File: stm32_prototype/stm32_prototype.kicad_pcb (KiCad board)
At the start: 2 copper layers, 53.3 x 22.9 mm, 48 parts, among them J1 USB-C, J2 Cortex-Debug, J3 SWD, J4 Qwiic, J5 Header_A, J6 Header_B, SW1 BOOT0, SW2 RESET, U1 STM32F103C8T6, U2 USBLC6-2SC6, U3 AP2112K-3.3, Y1 8MHz, Y2 32.768kHz

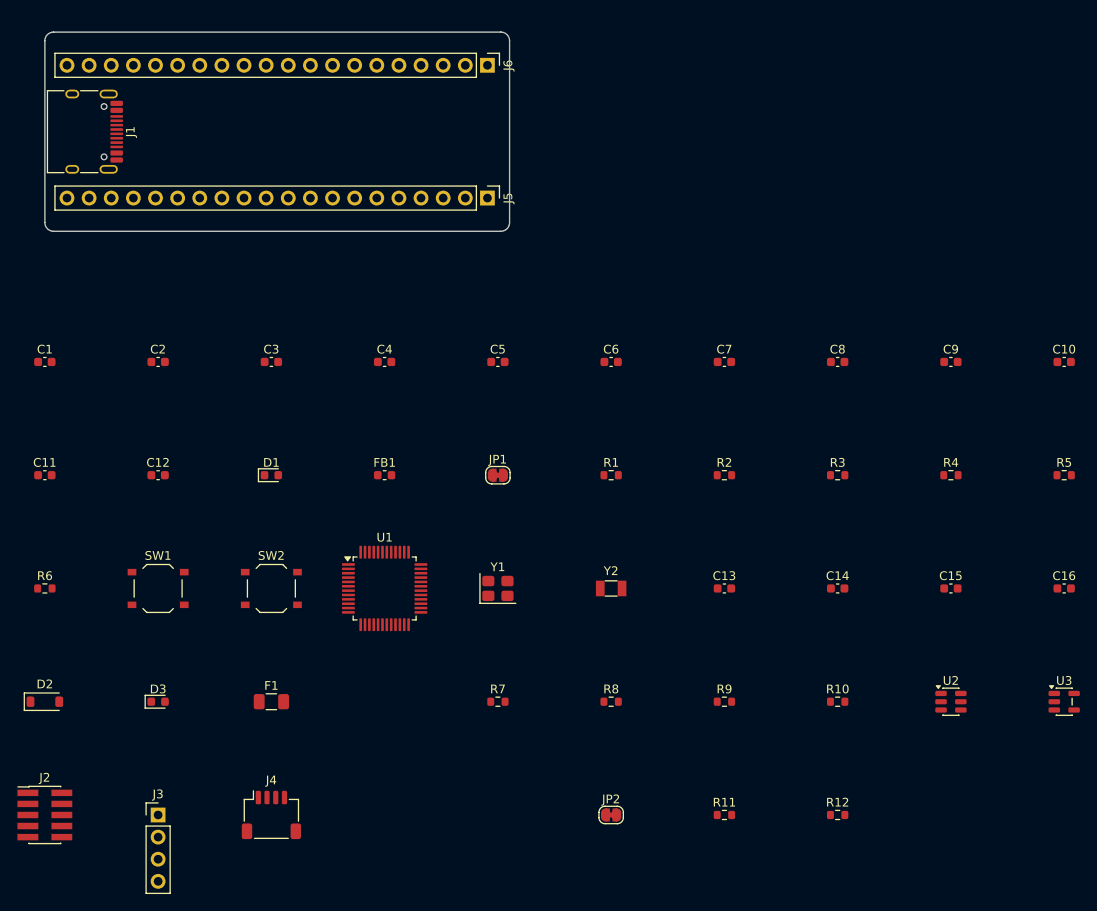
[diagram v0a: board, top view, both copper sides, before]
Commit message: Rev B placement: 76.2 x 22.86 mm board with Blue-Pill header pinout
- Headers centred; USB-C, ESD and power path in the left extension,
  Cortex-Debug, SWD and Qwiic in the right extension
- MCU rotated so PA11/PA12 face the USB connector; decoupling within 2-4 mm of
  the VDD pins, HSE crystal 3-5 mm from PD0/PD1
- Silk designators only on connectors, buttons, ICs and LEDs
- scripts/place_revb.py reproduces the placement

Co-Authored-By: Claude Opus 5.5 (1M context) <noreply@anthropic.com>
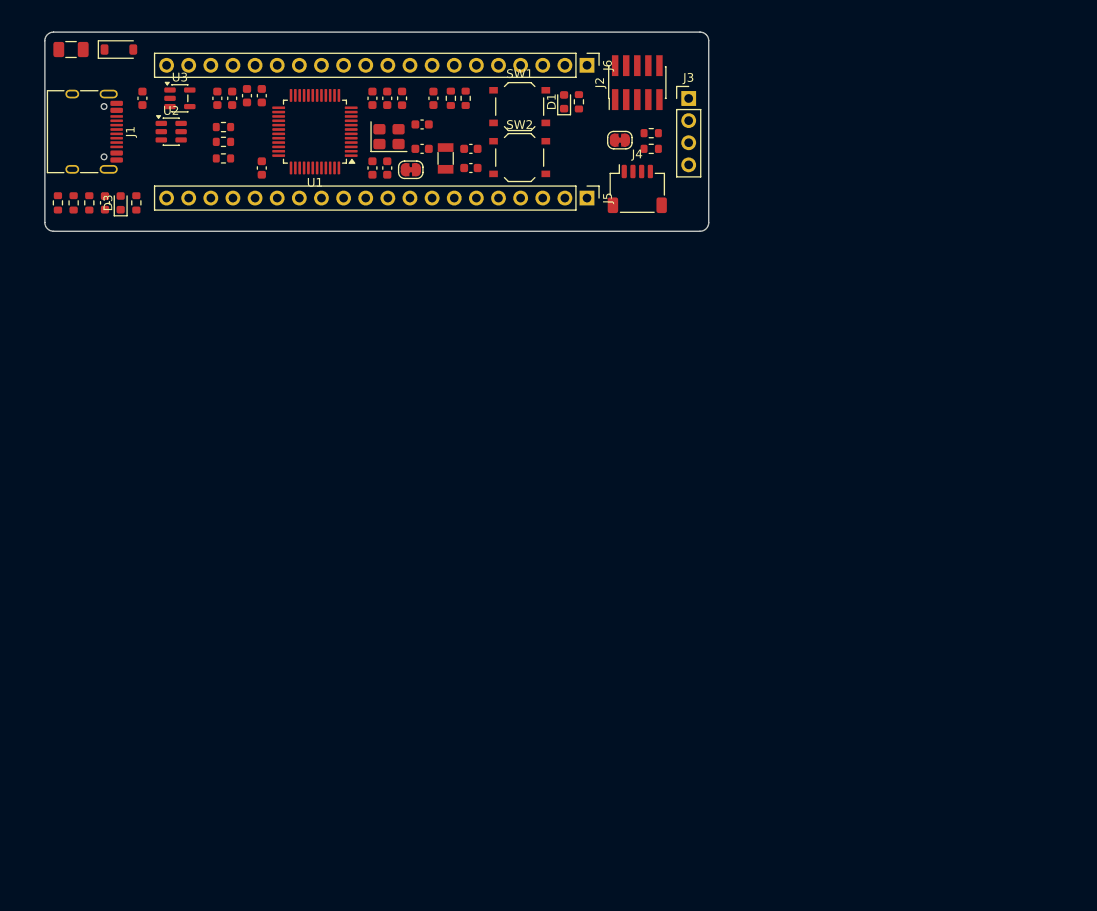
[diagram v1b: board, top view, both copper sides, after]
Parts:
- moved U3 122.9 mm to (115.5, 107.6)
- moved U2 110.9 mm to (114.5, 111.4)
- moved C16 110.8 mm to (121.5, 107.6), turned to 90 degrees
- moved J2 108.1 mm to (168.0, 105.8), turned to 90 degrees
- moved R5 103.8 mm to (120.5, 112.6)
- moved J3 102.3 mm to (173.9, 107.6)
- moved C15 101.3 mm to (119.8, 107.6), turned to 90 degrees
- moved R10 98.8 mm to (110.5, 119.6), turned to 90 degrees
- moved C14 97.6 mm to (111.2, 107.6), turned to 90 degrees
- moved R9 92.7 mm to (105.1, 119.6), turned to 90 degrees
- moved R4 92.6 mm to (120.5, 110.9)
- moved R8 84.2 mm to (103.3, 119.6), turned to 90 degrees
- moved C13 83.8 mm to (106.9, 119.6), turned to 90 degrees
- moved J4 83.2 mm to (168.0, 118.0)
- moved R12 79.4 mm to (169.6, 113.4)
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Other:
- board size 53.3 x 22.9 mm -> 76.2 x 22.9 mm

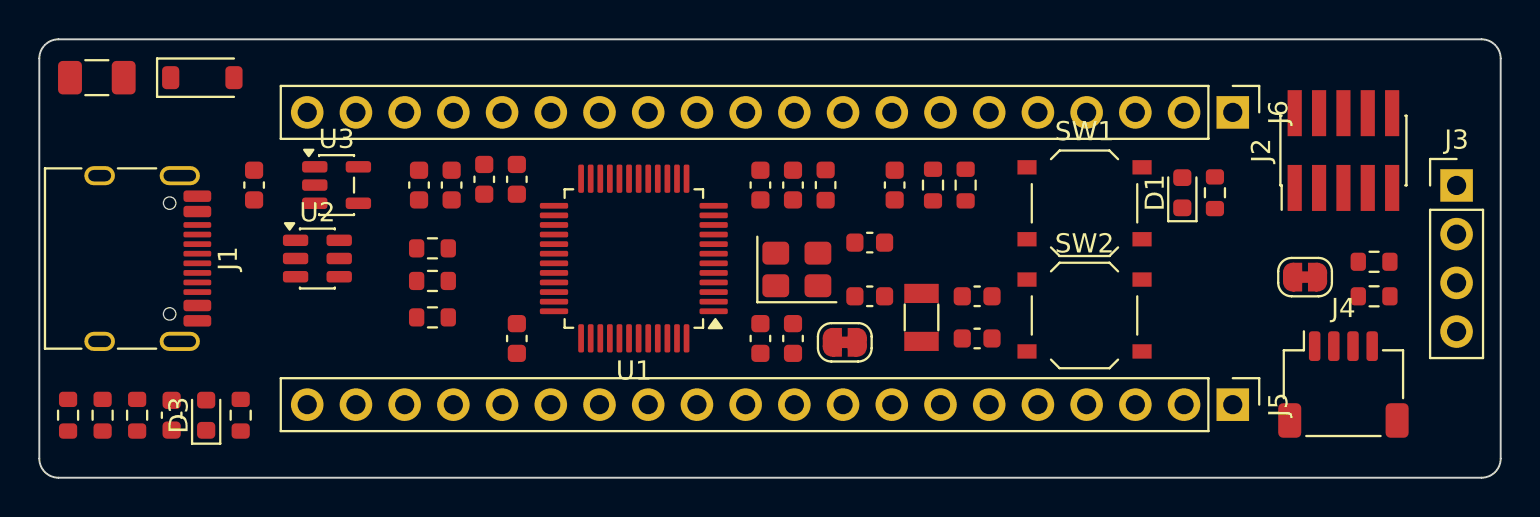
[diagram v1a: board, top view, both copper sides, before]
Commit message: Rev B routing: 4 layers SIG/GND/GND/SIG, Freerouting, GND pours, bottom pinout silk
- Freerouting 2.5 routes F.Cu/B.Cu with GND as a plane; vias modelled 0.7 mm so
  JLC's 0.5 mm hole-to-hole rule holds; board then converted to 4 layers with
  solid GND planes on In1/In2 and GND pours + edge stitching on F.Cu/B.Cu
- Net classes: Default/Supply clearance 0.15 mm (LQFP escape between the header rows),
  Supply class 0.3 mm for 3V3/GND/VDDA/VBAT
- Drop the USB skew rule (12 Mbit/s full speed is not length critical)
- Top designators hidden; pinout and connector labels on the bottom silkscreen
- DRC: 0 violations, 0 unconnected, 0 schematic parity issues
- scripts/route_revb.sh reproduces the whole routing step

Co-Authored-By: Claude Opus 5.5 (1M context) <noreply@anthropic.com>
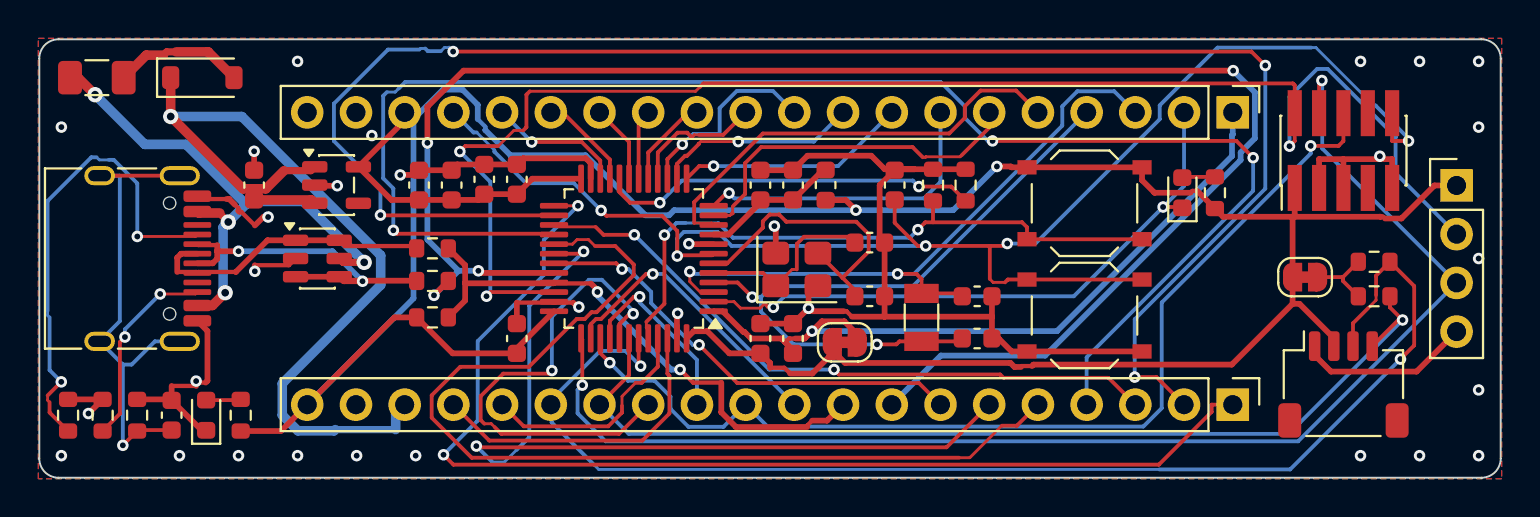
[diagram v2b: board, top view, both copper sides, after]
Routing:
- net +3V3: track 0.00 -> 163.4 mm, vias 0 -> 2
- net GND: track 0.00 -> 104.7 mm, vias 0 -> 31
- net PA11: track 0.00 -> 88.8 mm, vias 0 -> 4
- net PB13: track 0.00 -> 88.4 mm, vias 0 -> 4
- net PB15: track 0.00 -> 79.8 mm, vias 0 -> 3
- net NRST: track 0.00 -> 79.2 mm, vias 0 -> 5
- net SWDIO: track 0.00 -> 77.8 mm, vias 0 -> 3
- net SWCLK: track 0.00 -> 69.1 mm, vias 0 -> 2
- net I2C_SDA: track 0.00 -> 67.5 mm, vias 0 -> 2
- net PB12: track 0.00 -> 60.0 mm, vias 0 -> 2
- net SWO: track 0.00 -> 53.5 mm, vias 0 -> 2
- net PA8: track 0.00 -> 53.3 mm
- net I2C_SCL: track 0.00 -> 52.7 mm, vias 0 -> 1
- net +5V: track 0.00 -> 47.6 mm, vias 0 -> 1
- net PA9: track 0.00 -> 43.8 mm, vias 0 -> 2
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- added copper zone on B.Cu, net GND
- added copper zone on F.Cu, net GND
- added copper zone on In1.Cu, net GND
- added copper zone on In2.Cu, net GND
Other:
- copper layers 2 -> 4
- board text added: "3V3"
- board text added: "5V"
- board text added: "BOOT0"
- board text added: "DEBUG"
- board text added: "GND"
- board text added: "PA0"
- board text added: "PA1"
- board text added: "PA10"
- board text added: "PA11"
- board text added: "PA12"
- board text added: "PA15"
- board text added: "PA2"
- board text added: "PA3"
- board text added: "PA4"
- board text added: "PA5"
- board text added: "PA6"
- board text added: "PA7"
- board text added: "PA8"
- board text added: "PA9"
- board text added: "PB0"
- board text added: "PB1"
- board text added: "PB10"
- board text added: "PB11"
- board text added: "PB12"
- board text added: "PB13"
- board text added: "PB14"
- board text added: "PB15"
- board text added: "PB3"
- board text added: "PB4"
- board text added: "PB5"
- board text added: "PB6"
- board text added: "PB7"
- board text added: "PB8"
- board text added: "PB9"
- board text added: "PC13"
- board text added: "PC14"
- board text added: "PC15"
- board text added: "QWIIC"
- board text added: "RESET"
- board text added: "RST"
- board text added: "STM32F103 Rev B Blue-Pill pinout"
- board text added: "SWD"
- board text added: "USB-C"
- board text added: "VB"

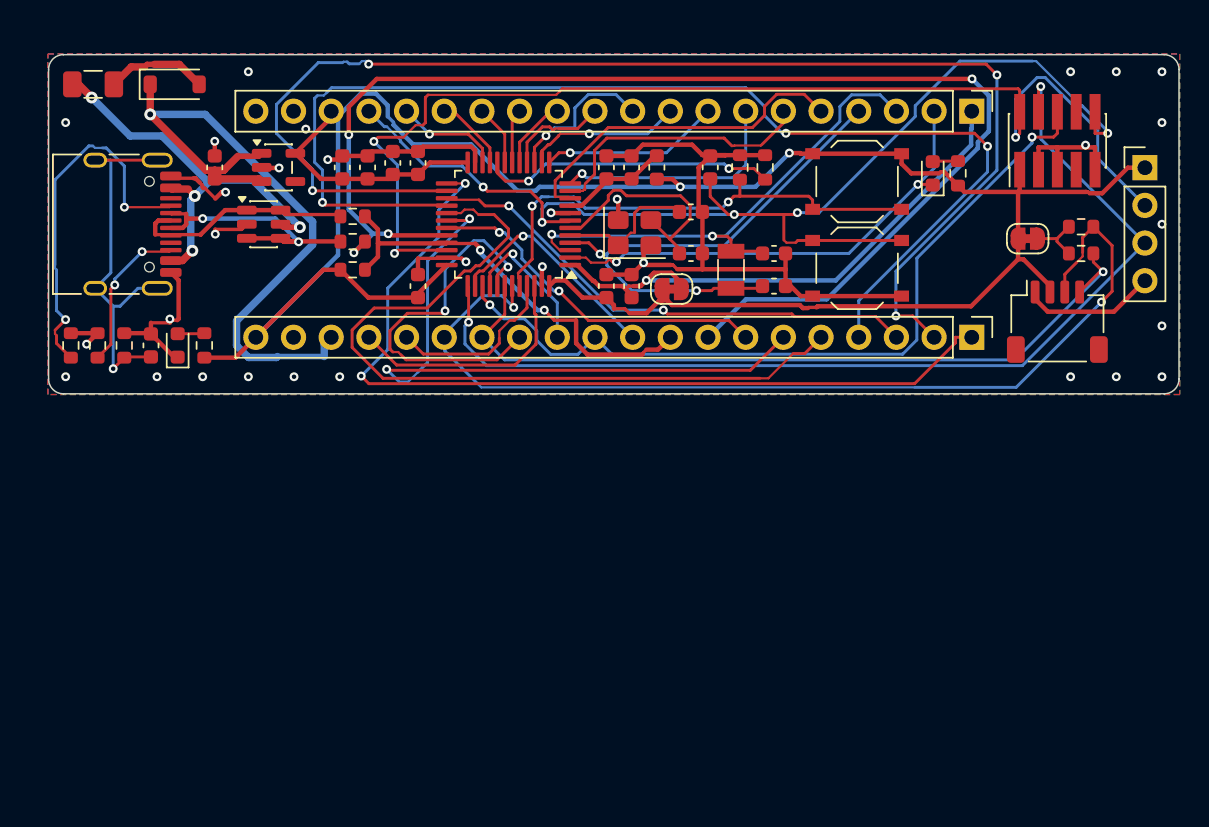
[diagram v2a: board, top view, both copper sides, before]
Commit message: Rev C board: 70 x 50 mm, M3 holes, net classes for motor/servo current, placement
Co-Authored-By: Claude Opus 5.5 (1M context) <noreply@anthropic.com>
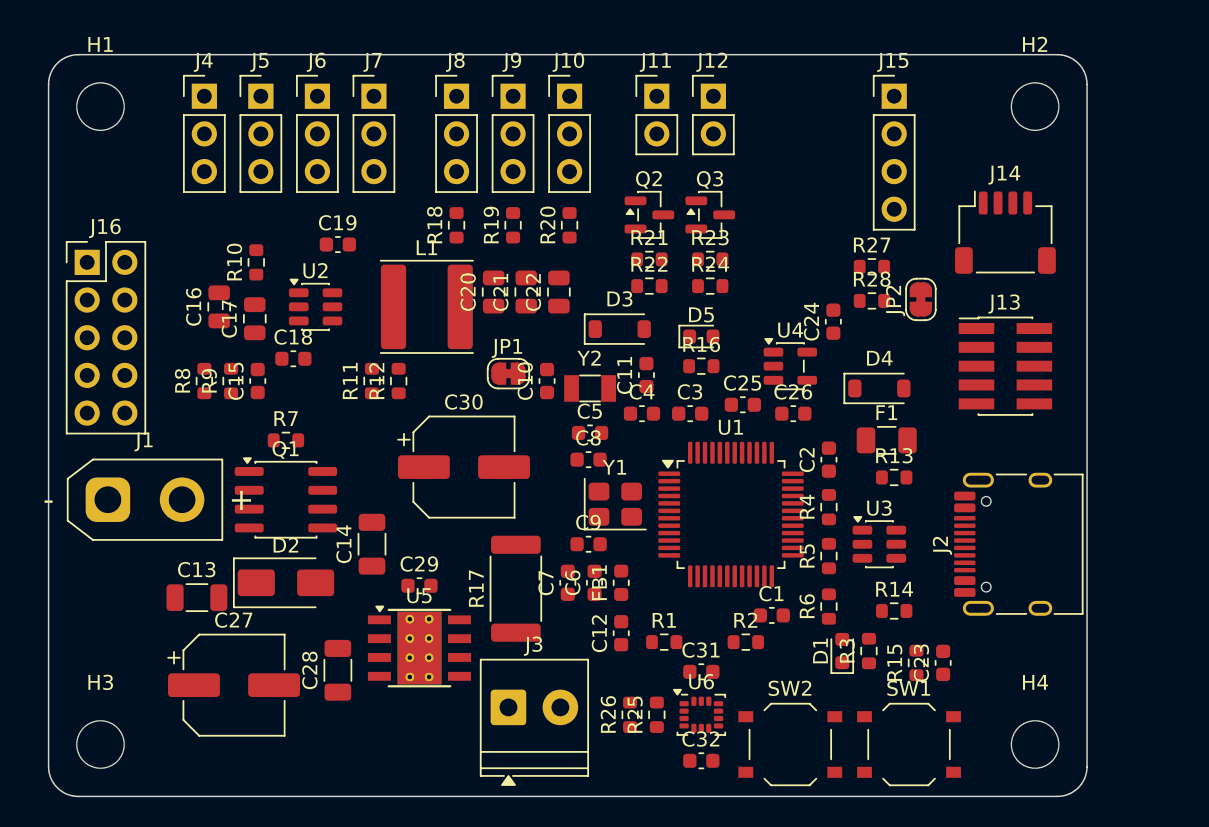
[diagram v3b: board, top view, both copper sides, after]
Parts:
- added C17: 10u 25V, Capacitor_SMD:C_0805_2012Metric, F.Cu at (113.9, 117.8)
- added C18: 100n, Capacitor_SMD:C_0603_1608Metric, F.Cu at (116.5, 120.5)
- added C19: 100n, Capacitor_SMD:C_0603_1608Metric, F.Cu at (119.5, 112.8)
- added C20: 22u 25V, Capacitor_SMD:C_0805_2012Metric, F.Cu at (130.0, 116.0)
- added C21: 22u 25V, Capacitor_SMD:C_0805_2012Metric, F.Cu at (132.2, 116.0)
- added C22: 22u 25V, Capacitor_SMD:C_0805_2012Metric, F.Cu at (134.4, 116.0)
- added C23: 4.7n, Capacitor_SMD:C_0603_1608Metric, F.Cu at (160.3, 141.0)
- added C24: 1u, Capacitor_SMD:C_0603_1608Metric, F.Cu at (152.9, 118.0)
- added C25: 1u, Capacitor_SMD:C_0603_1608Metric, F.Cu at (146.8, 123.6)
- added C26: 10u, Capacitor_SMD:C_0603_1608Metric, F.Cu at (150.2, 124.2)
- added C27: 100u 25V, Capacitor_SMD:CP_Elec_6.3x7.7, F.Cu at (112.5, 142.5)
- added C28: 22u 25V, Capacitor_SMD:C_1206_3216Metric, F.Cu at (119.5, 141.5)
- added C29: 100n, Capacitor_SMD:C_0603_1608Metric, F.Cu at (125.0, 135.8)
- added C30: 100u 25V, Capacitor_SMD:CP_Elec_6.3x7.7, F.Cu at (128.0, 127.8)
- added C31: 100n, Capacitor_SMD:C_0603_1608Metric, F.Cu at (144.0, 141.6)
- added C32: 100n, Capacitor_SMD:C_0603_1608Metric, F.Cu at (144.0, 147.6)
- added D4: B5819W, Diode_SMD:D_SOD-123, F.Cu at (156.0, 122.5)
- added D5: red, LED_SMD:LED_0603_1608Metric, F.Cu at (144.0, 119.0)
- added H1: M3, MountingHole:MountingHole_3.2mm_M3, F.Cu at (103.5, 103.5)
- added H2: M3, MountingHole:MountingHole_3.2mm_M3, F.Cu at (166.5, 103.5)
- added H3: M3, MountingHole:MountingHole_3.2mm_M3, F.Cu at (103.5, 146.5)
- added H4: M3, MountingHole:MountingHole_3.2mm_M3, F.Cu at (166.5, 146.5)
- added J10: RC3, Connector_PinHeader_2.54mm:PinHeader_1x03_P2.54mm_Vertical, F.Cu at (135.1, 102.8)
- added J11: LIGHT1, Connector_PinHeader_2.54mm:PinHeader_1x02_P2.54mm_Vertical, F.Cu at (141.0, 102.8)
- added J12: LIGHT2, Connector_PinHeader_2.54mm:PinHeader_1x02_P2.54mm_Vertical, F.Cu at (144.8, 102.8)
- added J13: Cortex-Debug, Connector_PinHeader_1.27mm:PinHeader_2x05_P1.27mm_Vertical_SMD, F.Cu at (164.5, 121.0)
- added J14: Qwiic, Connector_JST:JST_SH_SM04B-SRSS-TB_1x04-1MP_P1.00mm_Horizontal, F.Cu at (164.5, 112.0)
- added J15: UART, Connector_PinHeader_2.54mm:PinHeader_1x04_P2.54mm_Vertical, F.Cu at (157.0, 102.8)
- added J16: EXPANSION, Connector_PinHeader_2.54mm:PinHeader_2x05_P2.54mm_Vertical, F.Cu at (102.6, 114.0)
- added J7: SERVO4, Connector_PinHeader_2.54mm:PinHeader_1x03_P2.54mm_Vertical, F.Cu at (121.9, 102.8)
- added J8: RC1, Connector_PinHeader_2.54mm:PinHeader_1x03_P2.54mm_Vertical, F.Cu at (127.5, 102.8)
- added J9: RC2, Connector_PinHeader_2.54mm:PinHeader_1x03_P2.54mm_Vertical, F.Cu at (131.3, 102.8)
- added L1: 3.3u, Inductor_SMD:L_Sunlord_SWPA6045S, F.Cu at (125.5, 117.0)
- added Q1: AO4407A, Package_SO:SOIC-8_3.9x4.9mm_P1.27mm, F.Cu at (116.0, 130.0)
- added Q2: AO3400A, Package_TO_SOT_SMD:SOT-23, F.Cu at (140.5, 110.8)
- added Q3: AO3400A, Package_TO_SOT_SMD:SOT-23, F.Cu at (144.6, 110.8)
- added R13: 5.1k, Resistor_SMD:R_0603_1608Metric, F.Cu at (157.0, 128.5)
- added R14: 5.1k, Resistor_SMD:R_0603_1608Metric, F.Cu at (157.0, 137.5)
- added R15: 1M, Resistor_SMD:R_0603_1608Metric, F.Cu at (158.5, 141.0)
- added R16: 1k, Resistor_SMD:R_0603_1608Metric, F.Cu at (144.0, 121.0)
- added R17: 0.1R 2W, Resistor_SMD:R_2512_6332Metric, F.Cu at (131.5, 136.0)
- added R18: 1k, Resistor_SMD:R_0603_1608Metric, F.Cu at (127.5, 111.5)
- added R19: 1k, Resistor_SMD:R_0603_1608Metric, F.Cu at (131.3, 111.5)
- added R20: 1k, Resistor_SMD:R_0603_1608Metric, F.Cu at (135.1, 111.5)
- added R21: 100R, Resistor_SMD:R_0603_1608Metric, F.Cu at (140.5, 113.8)
- added R22: 100k, Resistor_SMD:R_0603_1608Metric, F.Cu at (140.5, 115.6)
- added R23: 100R, Resistor_SMD:R_0603_1608Metric, F.Cu at (144.6, 113.8)
- added R24: 100k, Resistor_SMD:R_0603_1608Metric, F.Cu at (144.6, 115.6)
- added R25: 10k, Resistor_SMD:R_0603_1608Metric, F.Cu at (141.0, 144.5)
- added R26: 10k, Resistor_SMD:R_0603_1608Metric, F.Cu at (139.2, 144.5)
- added R27: 4.7k, Resistor_SMD:R_0603_1608Metric, F.Cu at (155.5, 114.3)
- added R28: 4.7k, Resistor_SMD:R_0603_1608Metric, F.Cu at (155.5, 116.6)
- added U4: AP2112K-3.3, Package_TO_SOT_SMD:SOT-23-5, F.Cu at (150.0, 121.0)
- added U5: DRV8870, Package_SO:Texas_HSOP-8-1EP_3.9x4.9mm_P1.27mm_ThermalVias, F.Cu at (125.0, 140.0)
- added U6: LSM6DS3TR-C, Package_LGA:LGA-14_3x2.5mm_P0.5mm_LayoutBorder3x4y, F.Cu at (144.0, 144.5)
- C13: value 4.7n -> 22u 25V; footprint Capacitor_SMD:C_0603_1608Metric -> Capacitor_SMD:C_1206_3216Metric
- C14: value 1u -> 22u 25V; footprint Capacitor_SMD:C_0603_1608Metric -> Capacitor_SMD:C_1206_3216Metric
- C15: value 1u -> 100n
- C16: value 10u -> 10u 25V; footprint Capacitor_SMD:C_0603_1608Metric -> Capacitor_SMD:C_0805_2012Metric
- D2: value B5819W -> SMAJ15A; footprint Diode_SMD:D_SOD-123 -> Diode_SMD:D_SMA
- D3: value red -> B5819W; footprint LED_SMD:LED_0603_1608Metric -> Diode_SMD:D_SOD-123
- J1: value USB-C -> XT30 battery 2S-3S; footprint Connector_USB:USB_C_Receptacle_HRO_TYPE-C-31-M-12 -> Connector_AMASS:AMASS_XT30UPB-M_1x02_P5.0mm_Vertical
- J2: value Cortex-Debug -> USB-C; footprint Connector_PinHeader_1.27mm:PinHeader_2x05_P1.27mm_Vertical_SMD -> Connector_USB:USB_C_Receptacle_HRO_TYPE-C-31-M-12
- J3: value SWD -> MOTOR; footprint Connector_PinHeader_2.54mm:PinHeader_1x04_P2.54mm_Vertical -> TerminalBlock_Phoenix:TerminalBlock_Phoenix_PT-1,5-2-3.5-H_1x02_P3.50mm_Horizontal
- J4: value Qwiic -> SERVO1; footprint Connector_JST:JST_SH_SM04B-SRSS-TB_1x04-1MP_P1.00mm_Horizontal -> Connector_PinHeader_2.54mm:PinHeader_1x03_P2.54mm_Vertical
- J5: value Header_A -> SERVO2; footprint Connector_PinHeader_2.54mm:PinHeader_1x20_P2.54mm_Vertical -> Connector_PinHeader_2.54mm:PinHeader_1x03_P2.54mm_Vertical
- J6: value Header_B -> SERVO3; footprint Connector_PinHeader_2.54mm:PinHeader_1x20_P2.54mm_Vertical -> Connector_PinHeader_2.54mm:PinHeader_1x03_P2.54mm_Vertical
- R10: value 1k -> 100k
- R11: value 4.7k -> 56k
- R12: value 4.7k -> 10k
- R7: value 5.1k -> 10k
- R8: value 5.1k -> 33k
- R9: value 1M -> 10k
- U2: value USBLC6-2SC6 -> TPS563201; footprint Package_TO_SOT_SMD:SOT-23-6 -> Package_TO_SOT_SMD:TSOT-23-6
- U3: value AP2112K-3.3 -> USBLC6-2SC6; footprint Package_TO_SOT_SMD:SOT-23-5 -> Package_TO_SOT_SMD:SOT-23-6
- moved J4 59.5 mm to (110.5, 102.8)
- moved F1 58.6 mm to (156.5, 126.0)
- moved J3 56.2 mm to (131.0, 144.0)
- moved J5 50.6 mm to (114.3, 102.8), turned to 0 degrees
- moved R11 48.9 mm to (121.8, 122.0), turned to 90 degrees
- moved U3 47.8 mm to (156.0, 133.0)
- moved R12 46.8 mm to (123.6, 122.0), turned to 90 degrees
- moved J6 44.1 mm to (118.1, 102.8), turned to 0 degrees
- moved R6 39.3 mm to (152.6, 137.2), turned to 90 degrees
- moved C1 38.7 mm to (148.8, 137.8), turned to 0 degrees
- moved R5 38.5 mm to (152.6, 133.8), turned to 90 degrees
- moved SW1 38.1 mm to (158.0, 146.5)
- moved R4 37.6 mm to (152.6, 130.5), turned to 90 degrees
- moved D2 34.4 mm to (116.0, 135.6)
- moved D1 32.8 mm to (153.5, 140.2)
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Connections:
- C10 pad 1: PC14 -> /MCU/PC14
- C11 pad 1: PC15 -> /MCU/PC15
- C13 pad 1: /Power_USB/USB_SHIELD -> VBAT
- C14 pad 1: +5V -> VBAT
- C15 pad 1: +3V3 -> VBAT_SENSE
- C16 pad 1: +3V3 -> VBAT
- C5 pad 1: VBAT -> /MCU/VBAT_RTC
- D1 pad 1: PC13 -> /MCU/PC13
- D2 pad 1: +5V -> VBAT
- D2 pad 2: /Power_USB/VBUS_F -> GND
- D3 pad 1: GND -> +5V
- D3 pad 2: /Power_USB/LED_PWR_A -> V5_SERVO
- F1 pad 2: /Power_USB/VBUS_F -> /Power/VBUS_F
- J3 pad 1: +3V3 -> /Drive/MOTOR_A
- J3 pad 2: SWDIO -> /Drive/MOTOR_B
- J4 pad 1: GND -> SERVO1
- J4 pad 2: +3V3 -> V5_SERVO
- J4 pad 3: I2C_SDA -> GND
- J5 pad 1: PB12 -> SERVO2
- J5 pad 2: PB13 -> V5_SERVO
- J5 pad 3: PB14 -> GND
- J6 pad 1: VBAT -> SERVO3
- J6 pad 2: PC13 -> V5_SERVO
- J6 pad 3: PC14 -> GND
- JP1 pad 2: VBAT -> /MCU/VBAT_RTC
- JP2 pad 2: /Connectors/I2C_PU -> /IO/I2C_PU
- R10 pad 1: +3V3 -> VBAT
- R10 pad 2: /Power_USB/LED_PWR_A -> /Power/BUCK_EN
- R11 pad 1: /Connectors/I2C_PU -> V5_SERVO
- R11 pad 2: I2C_SDA -> /Power/BUCK_FB
- R12 pad 1: /Connectors/I2C_PU -> /Power/BUCK_FB
- R12 pad 2: I2C_SCL -> GND
- R4 pad 2: PA12 -> /MCU/PA12
- R5 pad 2: PA11 -> /MCU/PA11
- R6 pad 2: PA12 -> /MCU/PA12
- R7 pad 1: /Power_USB/CC1 -> /Power/Q_REV_G
- R8 pad 1: /Power_USB/CC2 -> VBAT
- R8 pad 2: GND -> VBAT_SENSE
- R9 pad 1: /Power_USB/USB_SHIELD -> VBAT_SENSE
- U1 pad 1: VBAT -> /MCU/VBAT_RTC
- U1 pad 10: PA0 -> SERVO1
- U1 pad 11: PA1 -> SERVO2
- U1 pad 12: PA2 -> SERVO3
- U1 pad 13: PA3 -> SERVO4
- U1 pad 14: PA4 -> VBAT_SENSE
- U1 pad 16: PA6 -> MOTOR_IN1
- U1 pad 17: PA7 -> MOTOR_IN2
- U1 pad 18: PB0 -> LIGHT1
- U1 pad 19: PB1 -> LIGHT2
- U1 pad 2: PC13 -> /MCU/PC13
- U1 pad 21: PB10 -> I2C_SCL
- U1 pad 22: PB11 -> I2C_SDA
- U1 pad 25: PB12 -> IMU_INT1
- U1 pad 26: PB13 -> IMU_INT2
- U1 pad 3: PC14 -> /MCU/PC14
- U1 pad 30: PA9 -> UART_TX
- U1 pad 31: PA10 -> UART_RX
- U1 pad 32: PA11 -> /MCU/PA11
- U1 pad 33: PA12 -> /MCU/PA12
- U1 pad 4: PC15 -> /MCU/PC15
- U1 pad 42: I2C_SCL -> RC_IN1
- U1 pad 43: I2C_SDA -> RC_IN2
- U1 pad 45: PB8 -> RC_IN3
- U2 pad 1: USB_D+ -> GND
- U2 pad 2: GND -> /Power/BUCK_SW
- U2 pad 3: USB_D- -> VBAT
- U2 pad 4: USB_D- -> /Power/BUCK_FB
- U2 pad 5: VBUS -> /Power/BUCK_EN
- U2 pad 6: USB_D+ -> /Power/BUCK_BST
- U3 pad 1: +5V -> USB_D+
- U3 pad 3: +5V -> USB_D-
- U3 pad 4: unconnected-(U3-NC-Pad4) -> USB_D-
- U3 pad 5: +3V3 -> VBUS
- Y2 pad 1: PC14 -> /MCU/PC14
- Y2 pad 2: PC15 -> /MCU/PC15
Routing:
- net +3V3: track 163.4 -> 0.00 mm, vias 2 -> 0
- net GND: track 104.7 -> 0.00 mm, vias 31 -> 0
- net PA11: track 88.8 -> 0.00 mm, vias 4 -> 0
- net PB13: track 88.4 -> 0.00 mm, vias 4 -> 0
- net PB15: track 79.8 -> 0.00 mm, vias 3 -> 0
- net NRST: track 79.2 -> 0.00 mm, vias 5 -> 0
- net SWDIO: track 77.8 -> 0.00 mm, vias 3 -> 0
- net SWCLK: track 69.1 -> 0.00 mm, vias 2 -> 0
- net I2C_SDA: track 67.5 -> 0.00 mm, vias 2 -> 0
- net PB12: track 60.0 -> 0.00 mm, vias 2 -> 0
- net SWO: track 53.5 -> 0.00 mm, vias 2 -> 0
- net PA8: track 53.3 -> 0.00 mm
- net I2C_SCL: track 52.7 -> 0.00 mm, vias 1 -> 0
- net +5V: track 47.6 -> 0.00 mm, vias 1 -> 0
- net PA9: track 43.8 -> 0.00 mm, vias 2 -> 0
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- removed copper zone on B.Cu, net GND
- removed copper zone on F.Cu, net GND
- removed copper zone on In1.Cu, net GND
- removed copper zone on In2.Cu, net GND
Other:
- board size 76.2 x 22.9 mm -> 70 x 50 mm
- copper layers 4 -> 2
- board text removed: "3V3"
- board text removed: "5V"
- board text removed: "BOOT0"
- board text removed: "DEBUG"
- board text removed: "GND"
- board text removed: "PA0"
- board text removed: "PA1"
- board text removed: "PA10"
- board text removed: "PA11"
- board text removed: "PA12"
- board text removed: "PA15"
- board text removed: "PA2"
- board text removed: "PA3"
- board text removed: "PA4"
- board text removed: "PA5"
- board text removed: "PA6"
- board text removed: "PA7"
- board text removed: "PA8"
- board text removed: "PA9"
- board text removed: "PB0"
- board text removed: "PB1"
- board text removed: "PB10"
- board text removed: "PB11"
- board text removed: "PB12"
- board text removed: "PB13"
- board text removed: "PB14"
- board text removed: "PB15"
- board text removed: "PB3"
- board text removed: "PB4"
- board text removed: "PB5"
- board text removed: "PB6"
- board text removed: "PB7"
- board text removed: "PB8"
- board text removed: "PB9"
- board text removed: "PC13"
- board text removed: "PC14"
- board text removed: "PC15"
- board text removed: "QWIIC"
- board text removed: "RESET"
- board text removed: "RST"
- board text removed: "STM32F103 Rev B Blue-Pill pinout"
- board text removed: "SWD"
- board text removed: "USB-C"
- board text removed: "VB"
